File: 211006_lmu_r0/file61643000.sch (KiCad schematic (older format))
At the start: 8 parts

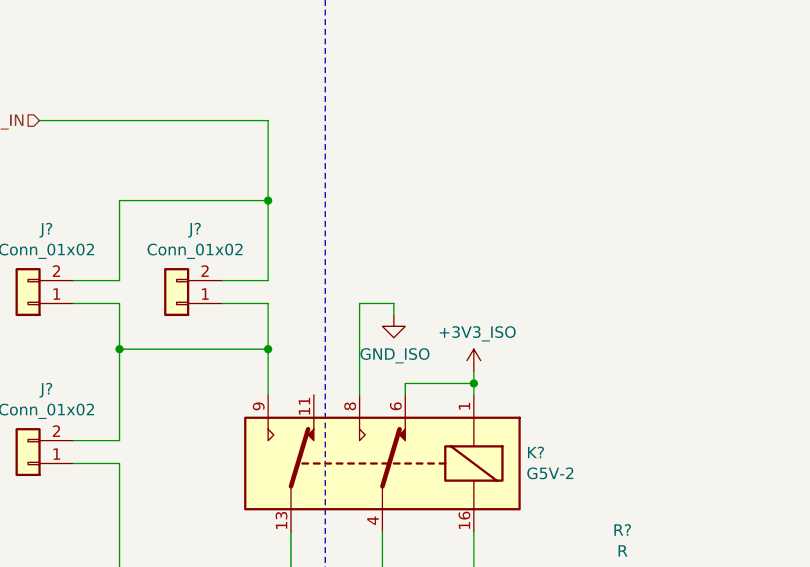
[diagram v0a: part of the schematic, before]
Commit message: inverted logic for the LMS fault detection relay
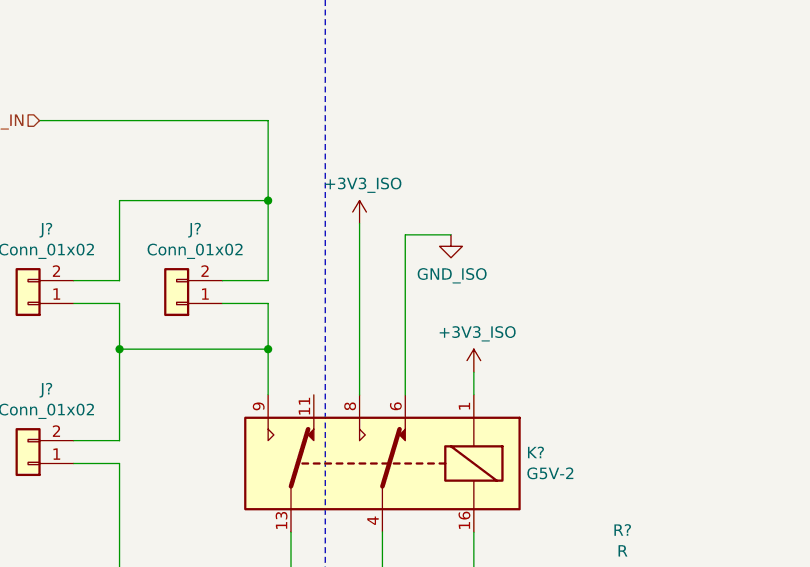
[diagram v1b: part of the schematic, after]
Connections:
- net +3V3: now also K?.8; no longer K?.6
- net GND: now also K?.6; no longer K?.8
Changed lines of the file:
@@
 $Descr A4 11693 8268
 encoding utf-8
-Sheet 32 35
+Sheet 31 35
 Title ""
 Date ""
@@
 $EndComp
 Wire Wire Line
-	5950 2800 5950 2850
-Wire Wire Line
 	5950 3500 5950 4000
 Wire Wire Line
@@
 L +3v3_iso:+3V3_ISO #PWR?
 U 1 1 616724FA
-P 5950 2800
-F 0 "#PWR?" H 5950 2650 50  0001 C CNN
-F 1 "+3V3_ISO" H 5965 2973 50  0000 C CNN
-F 2 "" H 5950 2800 50  0001 C CNN
-F 3 "" H 5950 2800 50  0001 C CNN
-	1    5950 2800
+P 5450 2150
+F 0 "#PWR?" H 5450 2000 50  0001 C CNN
+F 1 "+3V3_ISO" H 5465 2323 50  0000 C CNN
+F 2 "" H 5450 2150 50  0001 C CNN
+F 3 "" H 5450 2150 50  0001 C CNN
+	1    5450 2150
 	1    0    0    -1
 $EndComp
@@
 Wire Notes Line
 	5300 7750 5300 550
-Wire Wire Line
-	5650 2900 5650 2850
-Wire Wire Line
-	5650 2850 5950 2850
-Connection ~ 5950 2850
-Wire Wire Line
-	5950 2850 5950 2900
 $Comp
 L Device:R R?
@@
 Wire Wire Line
 	5550 3700 5550 3500
-$Comp
-L gnd_iso:GND_ISO #PWR?
-U 1 1 616783FF
-P 5600 2550
-F 0 "#PWR?" H 5600 2300 50  0001 C CNN
-F 1 "GND_ISO" H 5605 2377 50  0000 C CNN
-F 2 "" H 5600 2550 50  0001 C CNN
-F 3 "" H 5600 2550 50  0001 C CNN
-	1    5600 2550
-	1    0    0    -1
-$EndComp
-Wire Wire Line
-	5450 2900 5450 2500
-Wire Wire Line
-	5450 2500 5600 2500
-Wire Wire Line
-	5600 2500 5600 2550
 Text HLabel 7400 3700 2    50   Input ~ 0
 LMS_OK_FB
 Wire Wire Line
 	7400 3700 6750 3700
+Wire Wire Line
+	5950 2800 5950 2900
+Wire Wire Line
+	5450 2900 5450 2150
+$Comp
+L gnd_iso:GND_ISO #PWR?
+U 1 1 61F2F9D2
+P 5850 2200
+F 0 "#PWR?" H 5850 1950 50  0001 C CNN
+F 1 "GND_ISO" H 5855 2027 50  0000 C CNN
+F 2 "" H 5850 2200 50  0001 C CNN
+F 3 "" H 5850 2200 50  0001 C CNN
+	1    5850 2200
+	1    0    0    -1
+$EndComp
+Wire Wire Line
+	5650 2200 5850 2200
+Wire Wire Line
+	5650 2200 5650 2900
+$Comp
+L +3v3_iso:+3V3_ISO #PWR?
+U 1 1 61F30BD9
+P 5950 2800
+F 0 "#PWR?" H 5950 2650 50  0001 C CNN
+F 1 "+3V3_ISO" H 5965 2973 50  0000 C CNN
+F 2 "" H 5950 2800 50  0001 C CNN
+F 3 "" H 5950 2800 50  0001 C CNN
+	1    5950 2800
+	1    0    0    -1
+$EndComp
 $EndSCHEMATC

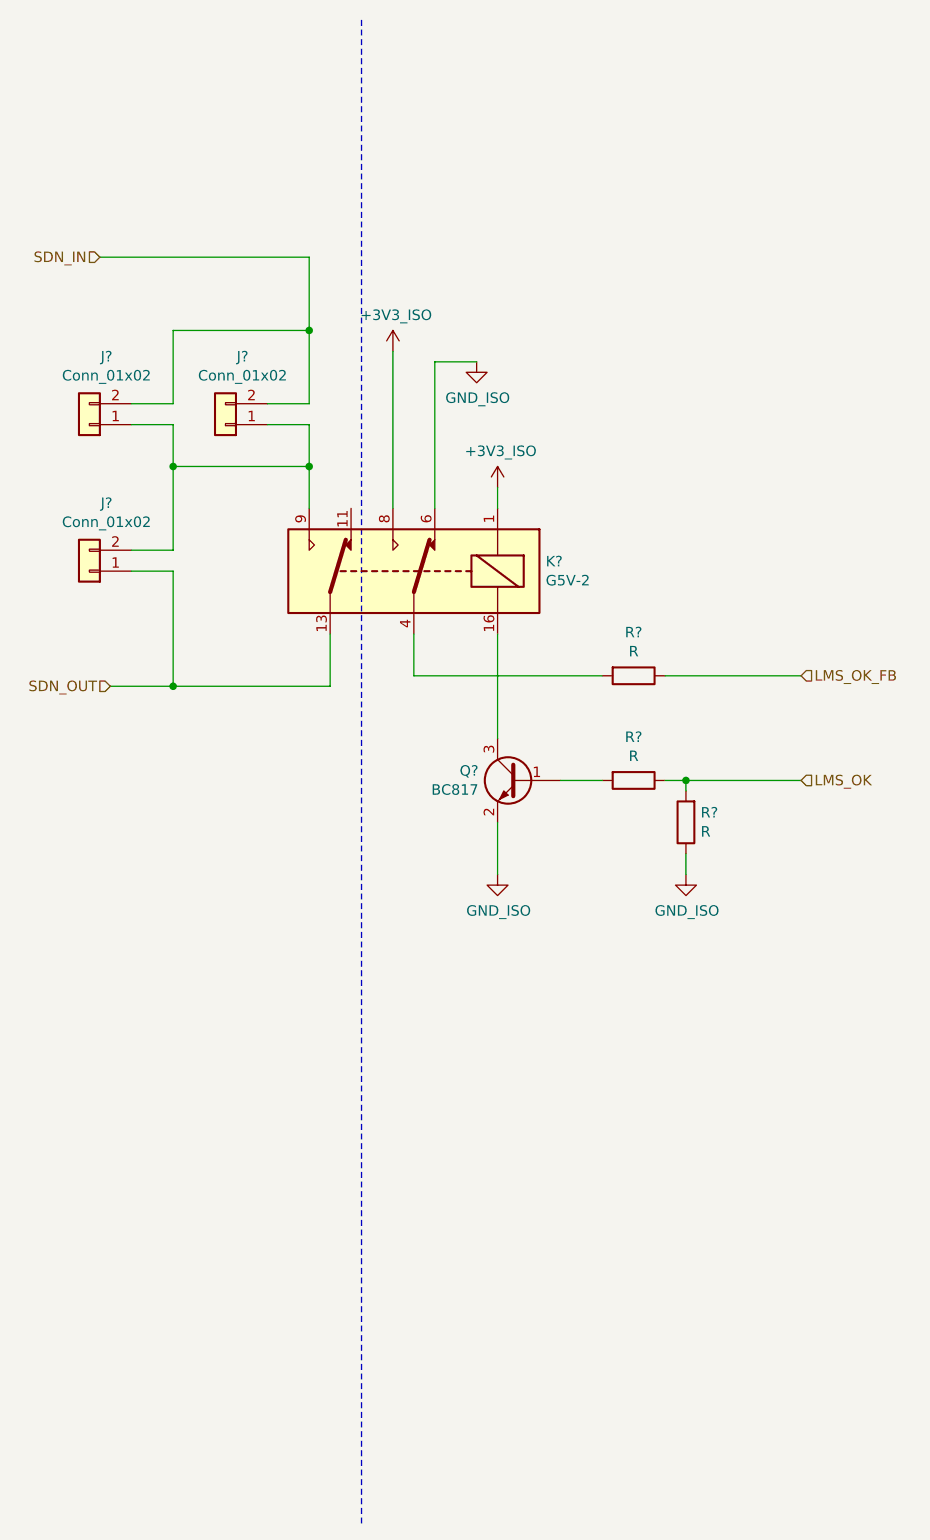
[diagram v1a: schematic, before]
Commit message: Updated BOM and footprints for non-hv components
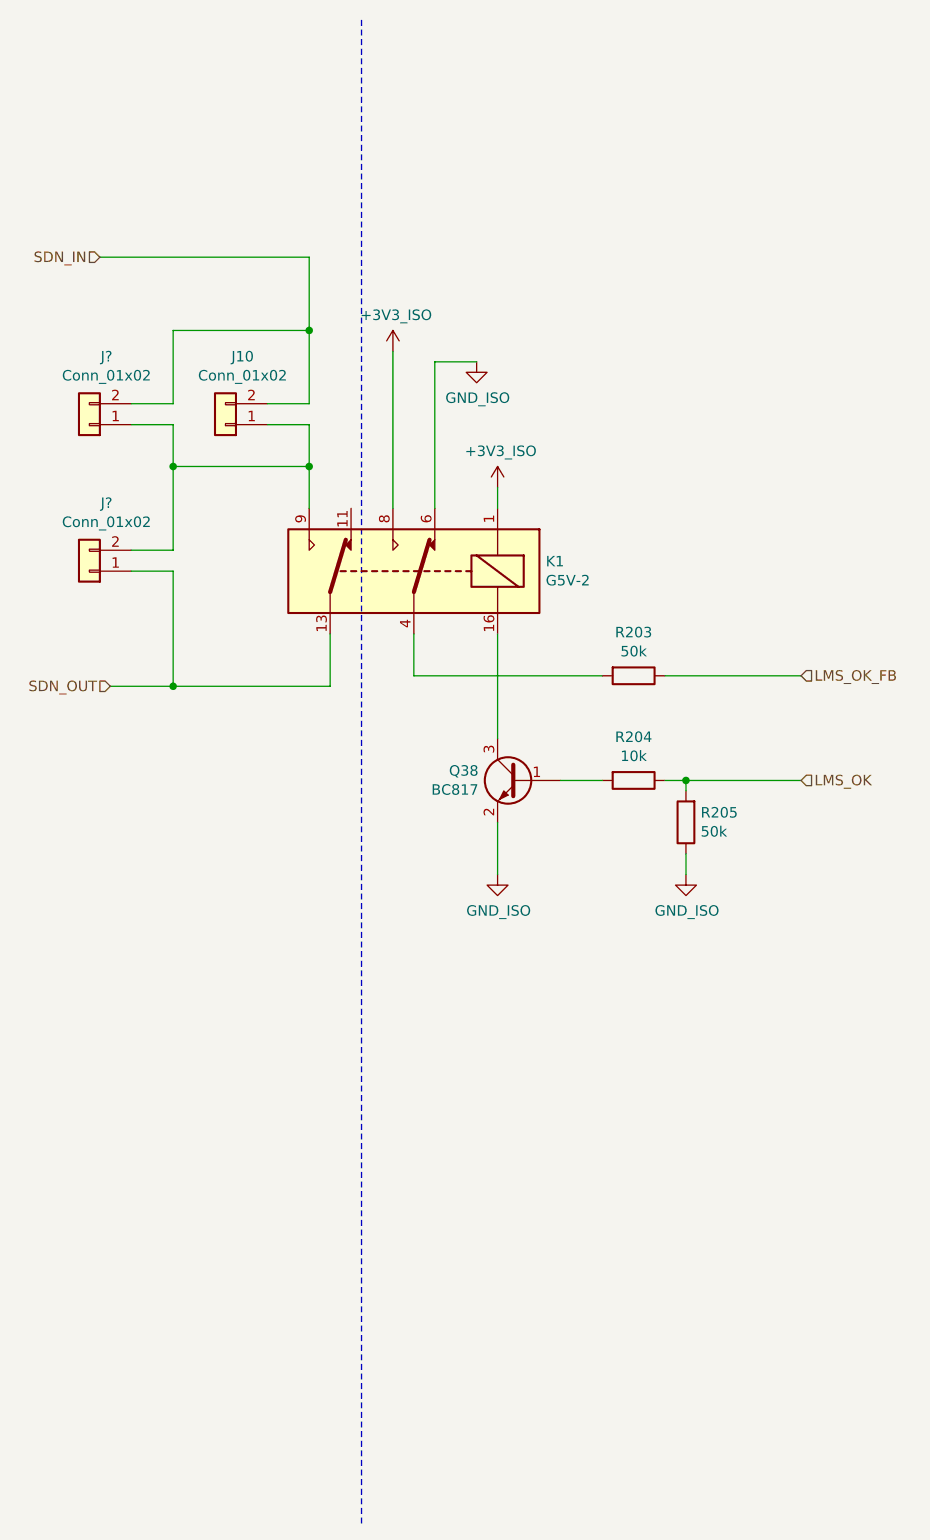
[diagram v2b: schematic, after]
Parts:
- removed J? (x2): Conn_01x02, symbol Connector_Generic:Conn_01x02
- added J? (x2): Conn_01x02, Connector_PinHeader_1.27mm:PinHeader_1x02_P1.27mm_Vertical, symbol Connector_Generic:Conn_01x02
- J10: renamed from J?; footprint (none) -> Connector_PinHeader_1.27mm:PinHeader_1x02_P1.27mm_Vertical
- R203, R205: renamed from R?; value R -> 50k; footprint (none) -> Resistor_SMD:R_0603_1608Metric_Pad0.98x0.95mm_HandSolder
- R204: renamed from R?; value R -> 10k; footprint (none) -> Resistor_SMD:R_0603_1608Metric_Pad0.98x0.95mm_HandSolder
- gave numbers to parts that had none: 2
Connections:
- net SDN_IN: now also J?.2 (Pin_2)
- net SDN_OUT: now also J?.1 (Pin_1)
- net at J10.1 (Pin_1), K1.9: now also J?.1 (Pin_1), J?.2 (Pin_2)
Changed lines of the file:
@@
 $EndDescr
 $Comp
-L Transistor_BJT:BC817 Q?
+L Transistor_BJT:BC817 Q38
 U 1 1 616435F7
 P 6050 4200
-F 0 "Q?" H 6241 4246 50  0000 L CNN
+F 0 "Q38" H 6241 4246 50  0000 L CNN
 F 1 "BC817" H 6241 4155 50  0000 L CNN
 F 2 "Package_TO_SOT_SMD:SOT-23" H 6250 4125 50  0001 L CIN
@@
 $EndComp
 $Comp
-L Device:R R?
+L Device:R R204
 U 1 1 61644D16
 P 6600 4200
-F 0 "R?" V 6393 4200 50  0000 C CNN
-F 1 "R" V 6484 4200 50  0000 C CNN
-F 2 "" V 6530 4200 50  0001 C CNN
+F 0 "R204" V 6393 4200 50  0000 C CNN
+F 1 "10k" V 6484 4200 50  0000 C CNN
+F 2 "Resistor_SMD:R_0603_1608Metric_Pad0.98x0.95mm_HandSolder" V 6530 4200 50  0001 C CNN
 F 3 "~" H 6600 4200 50  0001 C CNN
 	1    6600 4200
@@
 	5950 4400 5950 4650
 $Comp
-L Relay:G5V-2 K?
+L Relay:G5V-2 K1
 U 1 1 61647A5A
 P 5550 3200
-F 0 "K?" H 4920 3246 50  0000 R CNN
+F 0 "K1" H 4920 3246 50  0000 R CNN
 F 1 "G5V-2" H 4920 3155 50  0000 R CNN
 F 2 "Relay_THT:Relay_DPDT_Omron_G5V-2" H 6200 3150 50  0001 L CNN
@@
 SDN_OUT
 $Comp
-L Connector_Generic:Conn_01x02 J?
+L Connector_Generic:Conn_01x02 J10
 U 1 1 6164B7F9
 P 4650 2500
-F 0 "J?" H 4568 2175 50  0000 C CNN
+F 0 "J10" H 4568 2175 50  0000 C CNN
 F 1 "Conn_01x02" H 4568 2266 50  0000 C CNN
-F 2 "" H 4650 2500 50  0001 C CNN
+F 2 "Connector_PinHeader_1.27mm:PinHeader_1x02_P1.27mm_Vertical" H 4650 2500 50  0001 C CNN
 F 3 "~" H 4650 2500 50  0001 C CNN
 	1    4650 2500
@@
 Wire Wire Line
 	5050 1700 5050 2050
-$Comp
-L Connector_Generic:Conn_01x02 J?
-U 1 1 6164CDD1
-P 4000 2500
-F 0 "J?" H 3918 2175 50  0000 C CNN
-F 1 "Conn_01x02" H 3918 2266 50  0000 C CNN
-F 2 "" H 4000 2500 50  0001 C CNN
-F 3 "~" H 4000 2500 50  0001 C CNN
-	1    4000 2500
-	-1   0    0    1
-$EndComp
 Wire Wire Line
 	4200 2400 4400 2400
@@
 Wire Wire Line
 	5050 2700 5050 2900
-$Comp
-L Connector_Generic:Conn_01x02 J?
-U 1 1 6164DF7B
-P 4000 3200
-F 0 "J?" H 3918 2875 50  0000 C CNN
-F 1 "Conn_01x02" H 3918 2966 50  0000 C CNN
-F 2 "" H 4000 3200 50  0001 C CNN
-F 3 "~" H 4000 3200 50  0001 C CNN
-	1    4000 3200
-	-1   0    0    1
-$EndComp
 Wire Wire Line
 	4200 3100 4400 3100
@@
 	6850 4550 6850 4650
 $Comp
-L Device:R R?
+L Device:R R205
 U 1 1 6164548A
 P 6850 4400
-F 0 "R?" H 6780 4354 50  0000 R CNN
-F 1 "R" H 6780 4445 50  0000 R CNN
-F 2 "" V 6780 4400 50  0001 C CNN
+F 0 "R205" H 6780 4354 50  0000 R CNN
+F 1 "50k" H 6780 4445 50  0000 R CNN
+F 2 "Resistor_SMD:R_0603_1608Metric_Pad0.98x0.95mm_HandSolder" V 6780 4400 50  0001 C CNN
 F 3 "~" H 6850 4400 50  0001 C CNN
 	1    6850 4400
@@
 $EndComp
 $Comp
-L +3v3_iso:+3V3_ISO #PWR?
+L +3v3_iso:+3V3_ISO #PWR0166
 U 1 1 616724FA
 P 5450 2150
-F 0 "#PWR?" H 5450 2000 50  0001 C CNN
+F 0 "#PWR0166" H 5450 2000 50  0001 C CNN
 F 1 "+3V3_ISO" H 5465 2323 50  0000 C CNN
 F 2 "" H 5450 2150 50  0001 C CNN
@@
 $EndComp
 $Comp
-L gnd_iso:GND_ISO #PWR?
+L gnd_iso:GND_ISO #PWR0167
 U 1 1 61672BF9
 P 5950 4650
-F 0 "#PWR?" H 5950 4400 50  0001 C CNN
+F 0 "#PWR0167" H 5950 4400 50  0001 C CNN
 F 1 "GND_ISO" H 5955 4477 50  0000 C CNN
 F 2 "" H 5950 4650 50  0001 C CNN
@@
 $EndComp
 $Comp
-L gnd_iso:GND_ISO #PWR?
+L gnd_iso:GND_ISO #PWR0168
 U 1 1 61673215
 P 6850 4650
-F 0 "#PWR?" H 6850 4400 50  0001 C CNN
+F 0 "#PWR0168" H 6850 4400 50  0001 C CNN
 F 1 "GND_ISO" H 6855 4477 50  0000 C CNN
 F 2 "" H 6850 4650 50  0001 C CNN
@@
 	5300 7750 5300 550
 $Comp
-L Device:R R?
+L Device:R R203
 U 1 1 61677209
 P 6600 3700
-F 0 "R?" V 6393 3700 50  0000 C CNN
-F 1 "R" V 6484 3700 50  0000 C CNN
-F 2 "" V 6530 3700 50  0001 C CNN
+F 0 "R203" V 6393 3700 50  0000 C CNN
+F 1 "50k" V 6484 3700 50  0000 C CNN
+F 2 "Resistor_SMD:R_0603_1608Metric_Pad0.98x0.95mm_HandSolder" V 6530 3700 50  0001 C CNN
 F 3 "~" H 6600 3700 50  0001 C CNN
 	1    6600 3700
@@
 	5450 2900 5450 2150
 $Comp
-L gnd_iso:GND_ISO #PWR?
+L gnd_iso:GND_ISO #PWR0169
 U 1 1 61F2F9D2
 P 5850 2200
-F 0 "#PWR?" H 5850 1950 50  0001 C CNN
+F 0 "#PWR0169" H 5850 1950 50  0001 C CNN
 F 1 "GND_ISO" H 5855 2027 50  0000 C CNN
 F 2 "" H 5850 2200 50  0001 C CNN
@@
 	5650 2200 5650 2900
 $Comp
-L +3v3_iso:+3V3_ISO #PWR?
+L +3v3_iso:+3V3_ISO #PWR0170
 U 1 1 61F30BD9
 P 5950 2800
-F 0 "#PWR?" H 5950 2650 50  0001 C CNN
+F 0 "#PWR0170" H 5950 2650 50  0001 C CNN
 F 1 "+3V3_ISO" H 5965 2973 50  0000 C CNN
 F 2 "" H 5950 2800 50  0001 C CNN
@@
 	1    0    0    -1
 $EndComp
+$Comp
+L Connector_Generic:Conn_01x02 J?
+U 1 1 61F4C910
+P 4000 2500
+F 0 "J?" H 3918 2175 50  0000 C CNN
+F 1 "Conn_01x02" H 3918 2266 50  0000 C CNN
+F 2 "Connector_PinHeader_1.27mm:PinHeader_1x02_P1.27mm_Vertical" H 4000 2500 50  0001 C CNN
+F 3 "~" H 4000 2500 50  0001 C CNN
+	1    4000 2500
+	-1   0    0    1
+$EndComp
+$Comp
+L Connector_Generic:Conn_01x02 J?
+U 1 1 61F4CE6C
+P 4000 3200
+F 0 "J?" H 3918 2875 50  0000 C CNN
+F 1 "Conn_01x02" H 3918 2966 50  0000 C CNN
+F 2 "Connector_PinHeader_1.27mm:PinHeader_1x02_P1.27mm_Vertical" H 4000 3200 50  0001 C CNN
+F 3 "~" H 4000 3200 50  0001 C CNN
+	1    4000 3200
+	-1   0    0    1
+$EndComp
 $EndSCHEMATC

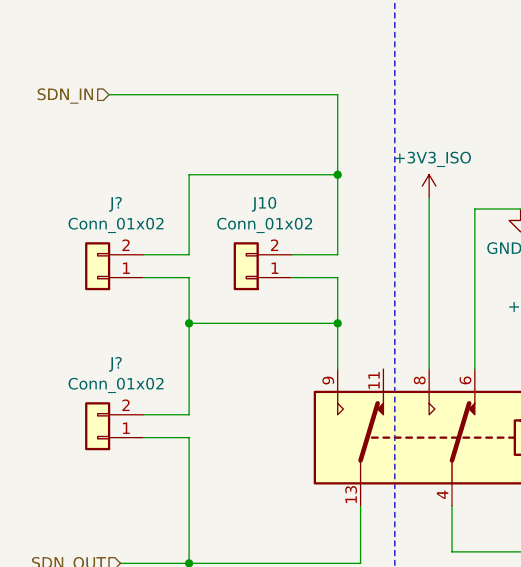
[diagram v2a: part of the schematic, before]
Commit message: Added most footprint requirements in HV
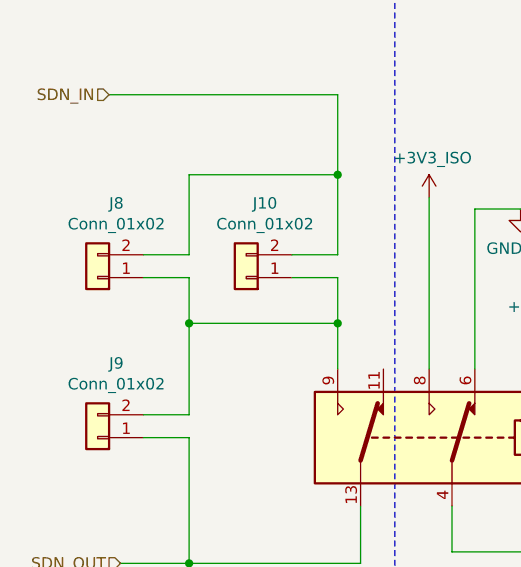
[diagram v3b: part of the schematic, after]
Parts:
- gave numbers to parts that had none: 2
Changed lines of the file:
@@
 $EndComp
 $Comp
-L +3v3_iso:+3V3_ISO #PWR0166
+L +3v3_iso:+3V3_ISO #PWR066
 U 1 1 616724FA
 P 5450 2150
-F 0 "#PWR0166" H 5450 2000 50  0001 C CNN
+F 0 "#PWR066" H 5450 2000 50  0001 C CNN
 F 1 "+3V3_ISO" H 5465 2323 50  0000 C CNN
 F 2 "" H 5450 2150 50  0001 C CNN
@@
 $EndComp
 $Comp
-L gnd_iso:GND_ISO #PWR0167
+L gnd_iso:GND_ISO #PWR069
 U 1 1 61672BF9
 P 5950 4650
-F 0 "#PWR0167" H 5950 4400 50  0001 C CNN
+F 0 "#PWR069" H 5950 4400 50  0001 C CNN
 F 1 "GND_ISO" H 5955 4477 50  0000 C CNN
 F 2 "" H 5950 4650 50  0001 C CNN
@@
 $EndComp
 $Comp
-L gnd_iso:GND_ISO #PWR0168
+L gnd_iso:GND_ISO #PWR070
 U 1 1 61673215
 P 6850 4650
-F 0 "#PWR0168" H 6850 4400 50  0001 C CNN
+F 0 "#PWR070" H 6850 4400 50  0001 C CNN
 F 1 "GND_ISO" H 6855 4477 50  0000 C CNN
 F 2 "" H 6850 4650 50  0001 C CNN
@@
 	5450 2900 5450 2150
 $Comp
-L gnd_iso:GND_ISO #PWR0169
+L gnd_iso:GND_ISO #PWR067
 U 1 1 61F2F9D2
 P 5850 2200
-F 0 "#PWR0169" H 5850 1950 50  0001 C CNN
+F 0 "#PWR067" H 5850 1950 50  0001 C CNN
 F 1 "GND_ISO" H 5855 2027 50  0000 C CNN
 F 2 "" H 5850 2200 50  0001 C CNN
@@
 	5650 2200 5650 2900
 $Comp
-L +3v3_iso:+3V3_ISO #PWR0170
+L +3v3_iso:+3V3_ISO #PWR068
 U 1 1 61F30BD9
 P 5950 2800
-F 0 "#PWR0170" H 5950 2650 50  0001 C CNN
+F 0 "#PWR068" H 5950 2650 50  0001 C CNN
 F 1 "+3V3_ISO" H 5965 2973 50  0000 C CNN
 F 2 "" H 5950 2800 50  0001 C CNN
@@
 $EndComp
 $Comp
-L Connector_Generic:Conn_01x02 J?
+L Connector_Generic:Conn_01x02 J8
 U 1 1 61F4C910
 P 4000 2500
-F 0 "J?" H 3918 2175 50  0000 C CNN
+F 0 "J8" H 3918 2175 50  0000 C CNN
 F 1 "Conn_01x02" H 3918 2266 50  0000 C CNN
 F 2 "Connector_PinHeader_1.27mm:PinHeader_1x02_P1.27mm_Vertical" H 4000 2500 50  0001 C CNN
@@
 $EndComp
 $Comp
-L Connector_Generic:Conn_01x02 J?
+L Connector_Generic:Conn_01x02 J9
 U 1 1 61F4CE6C
 P 4000 3200
-F 0 "J?" H 3918 2875 50  0000 C CNN
+F 0 "J9" H 3918 2875 50  0000 C CNN
 F 1 "Conn_01x02" H 3918 2966 50  0000 C CNN
 F 2 "Connector_PinHeader_1.27mm:PinHeader_1x02_P1.27mm_Vertical" H 4000 3200 50  0001 C CNN
